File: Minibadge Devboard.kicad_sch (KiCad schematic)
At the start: 42 parts, among them J1 External power, J2 External switch, SW1 Power, SW3 SPEED, SW4 NTC

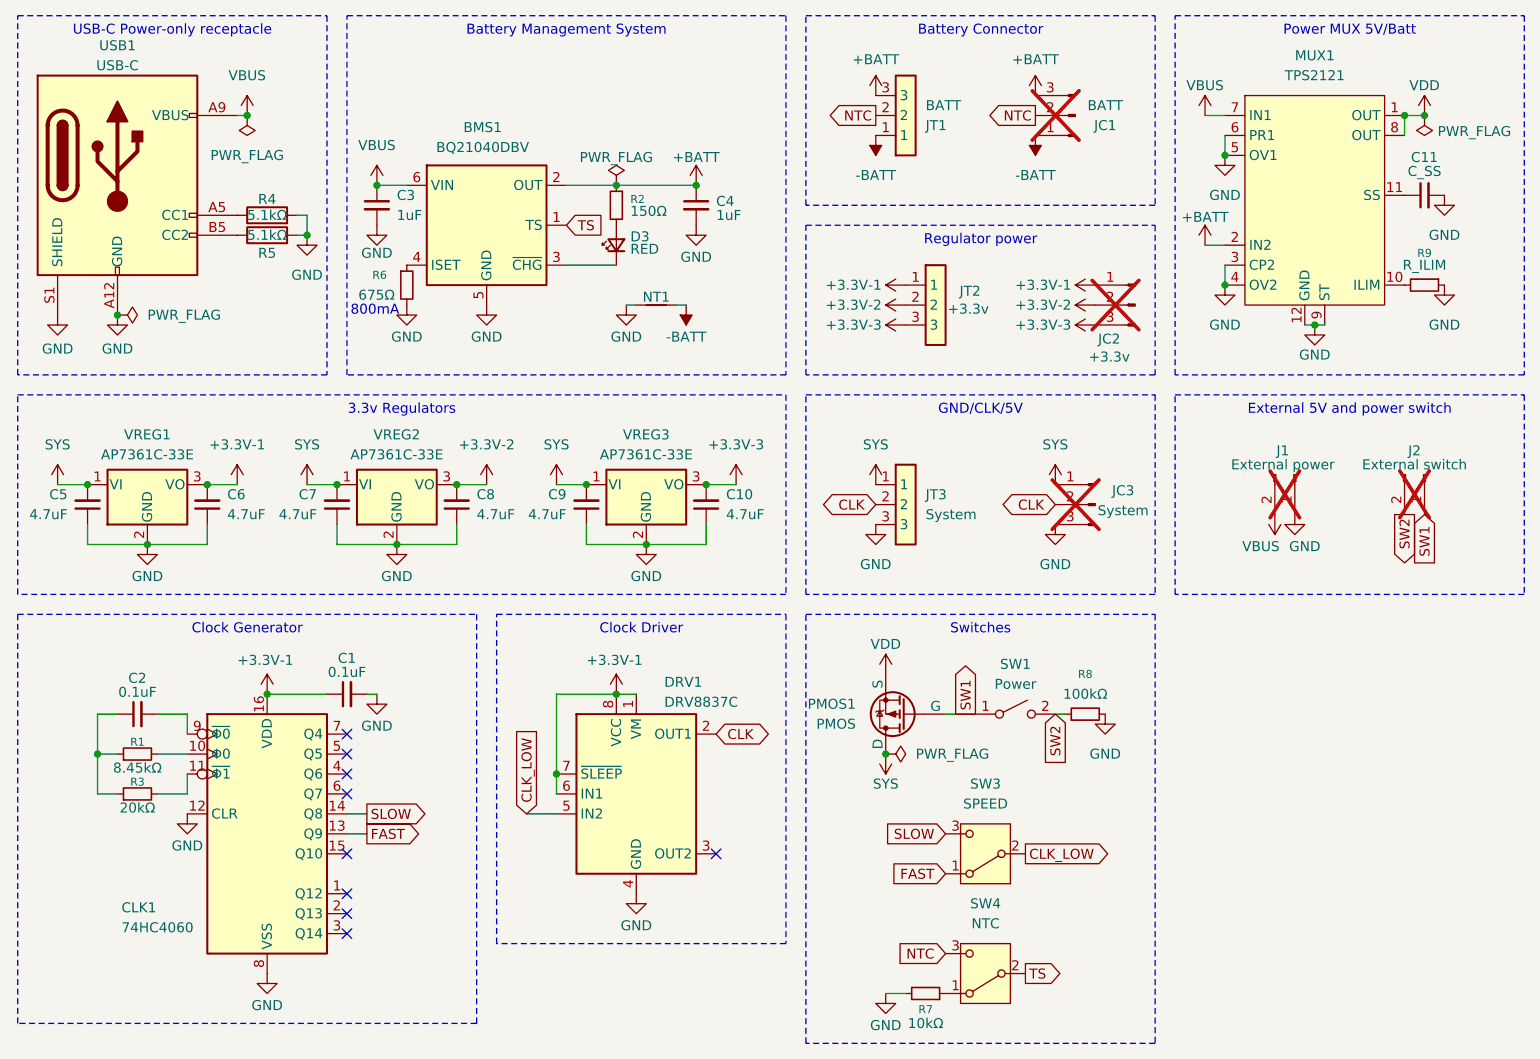
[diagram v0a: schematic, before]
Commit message: Add more LEDs to schematic
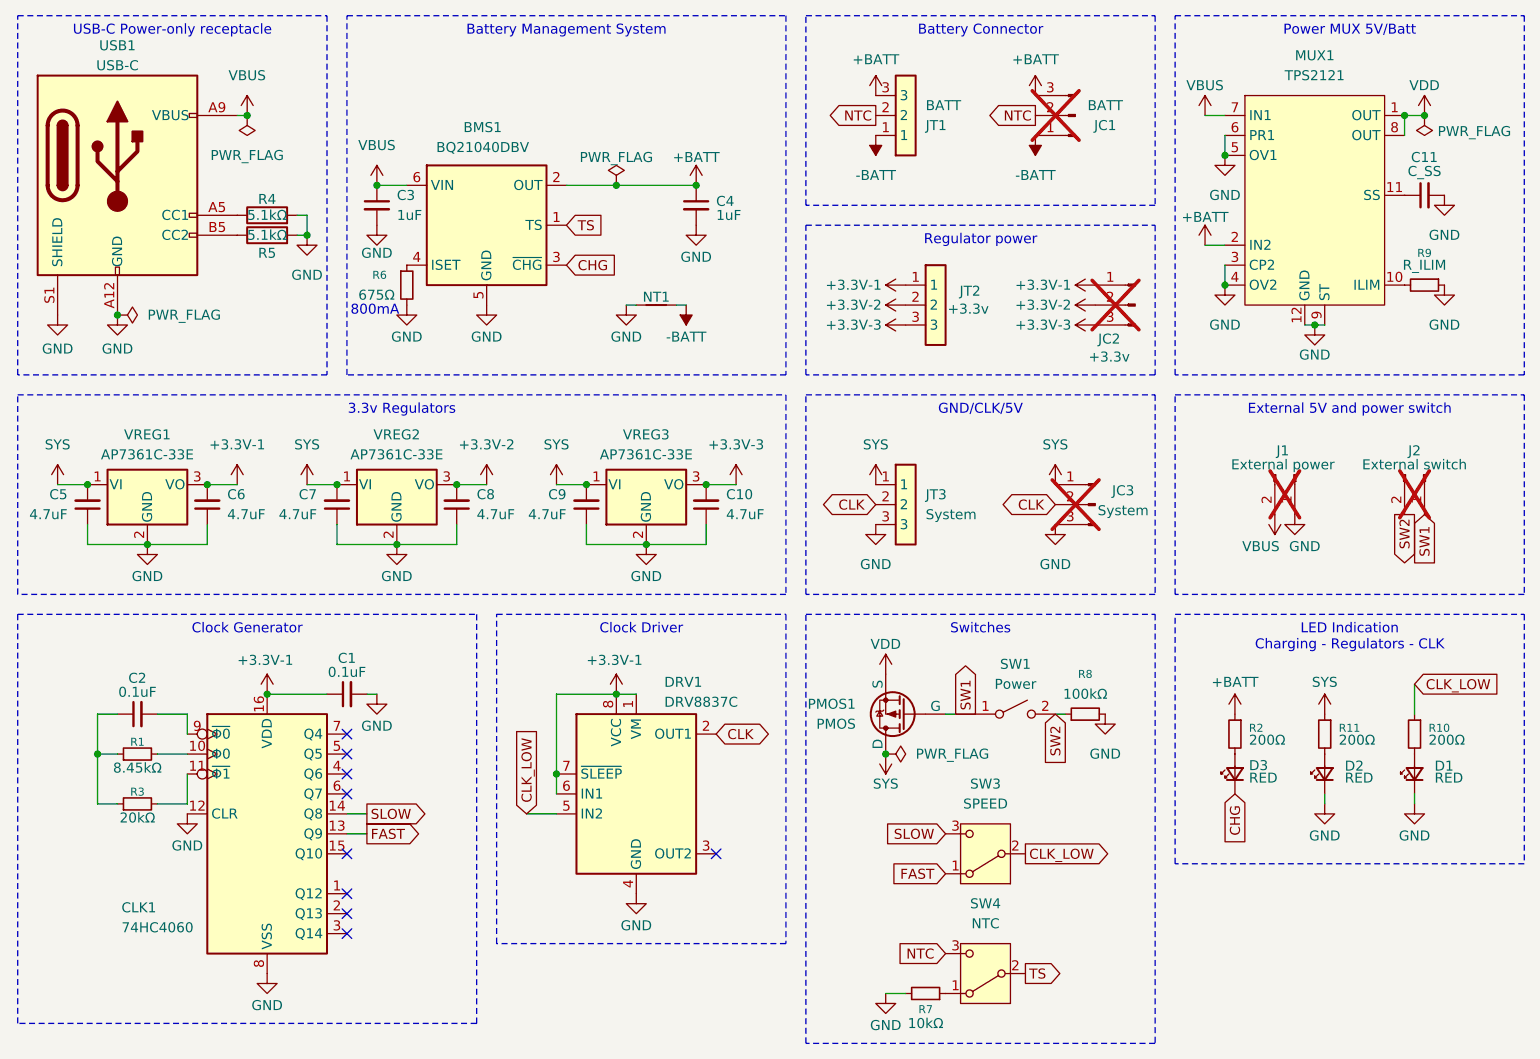
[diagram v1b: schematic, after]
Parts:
- added D1, D2: RED, LED_SMD:LED_0603_1608Metric, symbol Device:LED_Small
- added R10, R11: 200Ω, Resistor_SMD:R_0603_1608Metric, symbol Device:R_Small
- R2: value 150Ω -> 200Ω
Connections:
- net CLK_LOW: now also R10.1
- net GND: now also D1.1 (K), D2.1 (K)
- net SYS: now also R11.1
- net CHG: now reaches BMS1.3 (~{CHG}), D3.1 (K)
- new net: D2.2 (A), R11.2
- new net: D1.2 (A), R10.2
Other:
- moved on the sheet: D3, R2, R3

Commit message: Add LCSC part numbers
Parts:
- D1, D2: LCSC Part # (none) -> C2286
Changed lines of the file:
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@@
 			)
 		)
-		(property "LCSC Part #" ""
+		(property "LCSC Part #" "C2286"
 			(at 224.79 119.38 0)
 			(effects
@@
 			)
 		)
-		(property "LCSC Part #" ""
+		(property "LCSC Part #" "C2286"
 			(at 236.22 119.38 0)
 			(effects

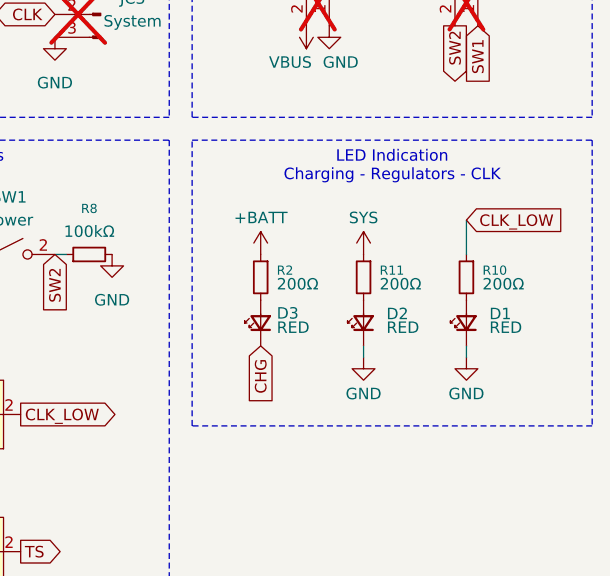
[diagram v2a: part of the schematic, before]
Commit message: Indicators and silkscreen
* Adjusted all passive component silkscreen thickness.
* Added labels for batt charging and system power.
* Added LED for system power.
* Adjusted positioning for several components.
* Swapped F and S CLK speed jumper text.
* Removed CLK indicator (could not fit)
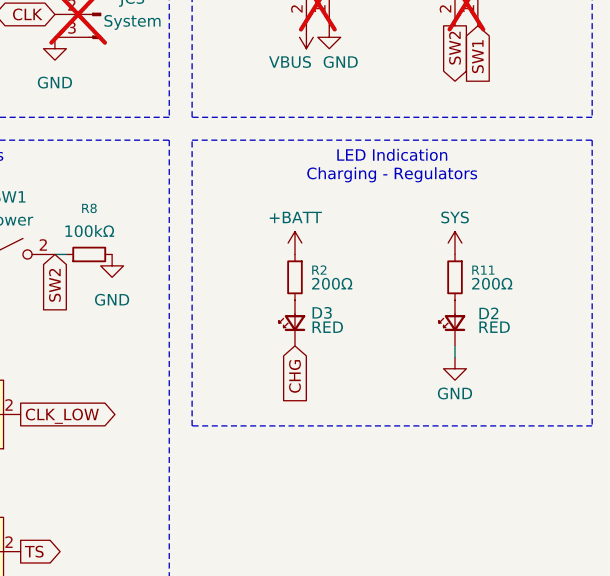
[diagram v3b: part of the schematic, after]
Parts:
- removed D1: RED, LED_SMD:LED_0603_1608Metric, symbol Device:LED_Small
- removed R10: 200Ω, Resistor_SMD:R_0603_1608Metric, symbol Device:R_Small
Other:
- moved on the sheet: D2, D3, R11, R2

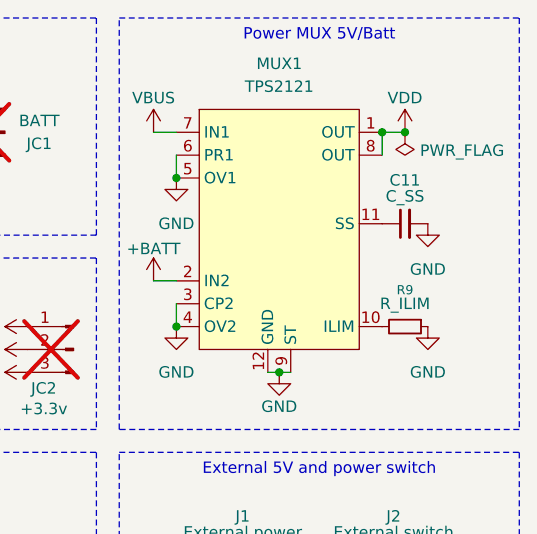
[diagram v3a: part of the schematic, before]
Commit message: Calculate ILIM and SS for MUX
Added LCSC numbers for new parts as well
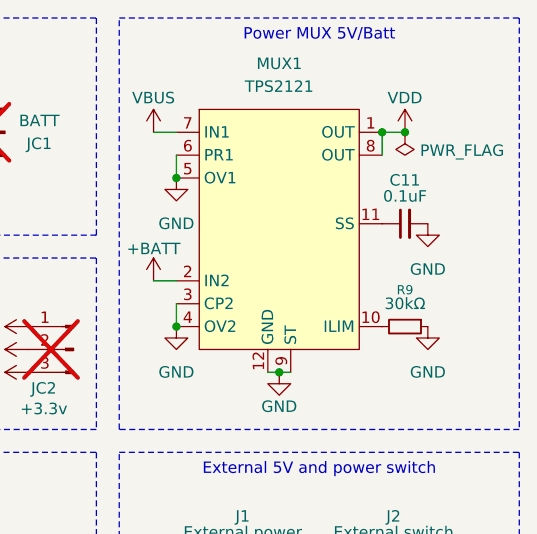
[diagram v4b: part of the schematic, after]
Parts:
- C11: value C_SS -> 0.1uF; LCSC Part # (none) -> C14663
- R11, R2: LCSC Part # (none) -> C8218
- R9: value R_ILIM -> 30kΩ; LCSC Part # (none) -> C22984
